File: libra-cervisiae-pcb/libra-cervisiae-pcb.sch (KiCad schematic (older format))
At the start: 23 parts, among them CN1 CP2102-BREAKOUT, CN2 HX711_BREAKOUT, J1 Wort Temp, J2 Board Temp, J3 Conn_02x08_Top_Bottom, SW1 Reset, SW2 Flash, U1 ESP-12F, U2 VREG

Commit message: PCB 0.2.0 release
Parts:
- J2: value Board Temp -> Ambient Temp; footprint Package_TO_SOT_THT:TO-92 -> Connector_PinHeader_2.54mm:PinHeader_1x03_P2.54mm_Vertical
- J3: value Conn_02x08_Top_Bottom -> Load Cells
- R2: value 10k -> 2.2k
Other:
- note added: "1"
- note added: "2"
- note added: "3"
- note added: "4"
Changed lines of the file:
@@
 Sheet 1 1
 Title "Libra Cervisiae PCB"
-Date "2018-08-09"
-Rev "0.1.2"
+Date "2018-08-31"
+Rev "0.2.0"
 Comp ""
 Comment1 ""
@@
 P 3750 5350
 F 0 "R2" V 3830 5350 50  0000 C CNN
-F 1 "10k" V 3750 5350 50  0000 C CNN
+F 1 "2.2k" V 3750 5350 50  0000 C CNN
 F 2 "Resistor_SMD:R_0805_2012Metric" V 3680 5350 50  0001 C CNN
 F 3 "" H 3750 5350 50  0001 C CNN
@@
 P 2950 5850
 F 0 "J2" H 2950 6050 50  0000 C CNN
-F 1 "Board Temp" H 2950 5650 50  0000 C CNN
-F 2 "Package_TO_SOT_THT:TO-92" H 2950 5850 50  0001 C CNN
+F 1 "Ambient Temp" H 2950 5650 50  0000 C CNN
+F 2 "Connector_PinHeader_2.54mm:PinHeader_1x03_P2.54mm_Vertical" H 2950 5850 50  0001 C CNN
 F 3 "" H 2950 5850 50  0001 C CNN
 	1    2950 5850
@@
 P 8750 5150
 F 0 "J3" H 8800 5667 50  0000 C CNN
-F 1 "Conn_02x08_Top_Bottom" H 8800 5576 50  0000 C CNN
+F 1 "Load Cells" H 8800 5576 50  0000 C CNN
 F 2 "Connector_PinHeader_2.54mm:PinHeader_2x08_P2.54mm_Vertical" H 8750 5150 50  0001 C CNN
 F 3 "~" H 8750 5150 50  0001 C CNN
@@
 Wire Wire Line
 	8400 4950 8550 4950
+Text Notes 8350 5000 2    60   ~ 0
+1
+Text Notes 8350 5400 2    60   ~ 0
+2
+Text Notes 9300 5000 2    60   ~ 0
+3
+Text Notes 9300 5400 2    60   ~ 0
+4
 $EndSCHEMATC

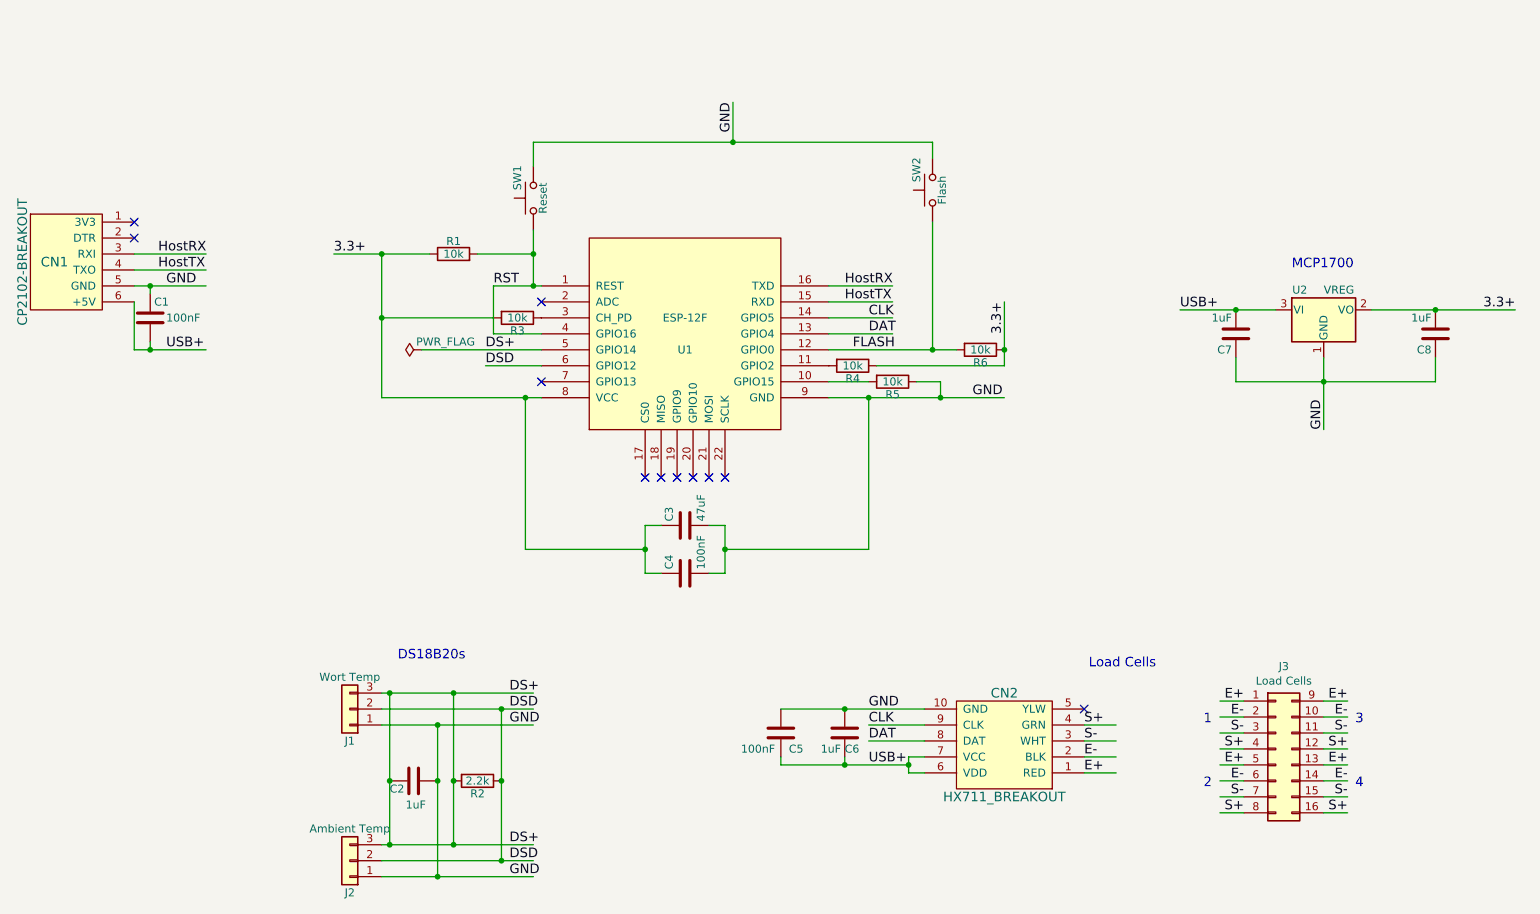
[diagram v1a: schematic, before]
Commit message: Schematic and layout for ESP32 version
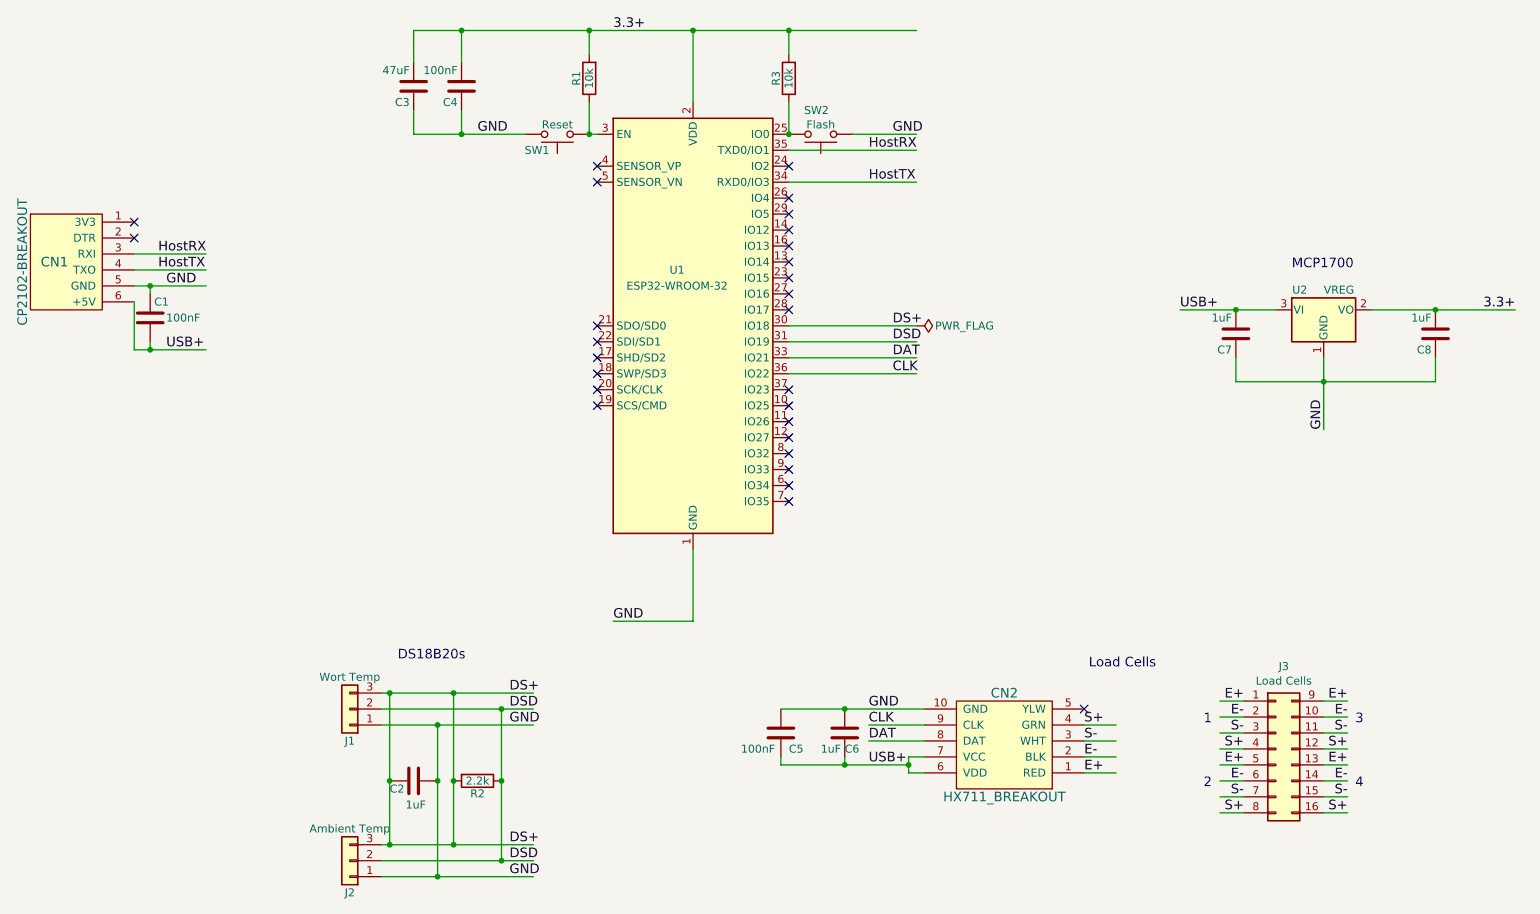
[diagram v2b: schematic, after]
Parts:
- removed R4, R5, R6: 10k, Resistor_SMD:R_0805_2012Metric, symbol Device:R
- removed U1: ESP-12F, ESP8266:ESP-12E, symbol ESP8266:ESP-12F
- added U1: ESP32-WROOM-32, RF_Module:ESP32-WROOM-32, symbol RF_Module:ESP32-WROOM-32
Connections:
- net labels removed: FLASH, RST
- wire segments 122 -> 99
- no-connect marks 11 -> 28
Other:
- moved on the sheet: C3, C4
